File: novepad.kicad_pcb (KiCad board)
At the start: 4 copper layers, 99 x 58 mm, 142 parts, among them J101 NOVENA_LCD_CONN, J102 LP097QX1_CONN, J401 MOLEX_502250-8037, J402 MOLEX_502250-8037, U201 TPS61181, U202 TPS61181, U301 IT6251, U401 FT5816LPC, X301 27MHz 50ppm, 8-18pF, ESR < 80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, X401 12MHz 18pF

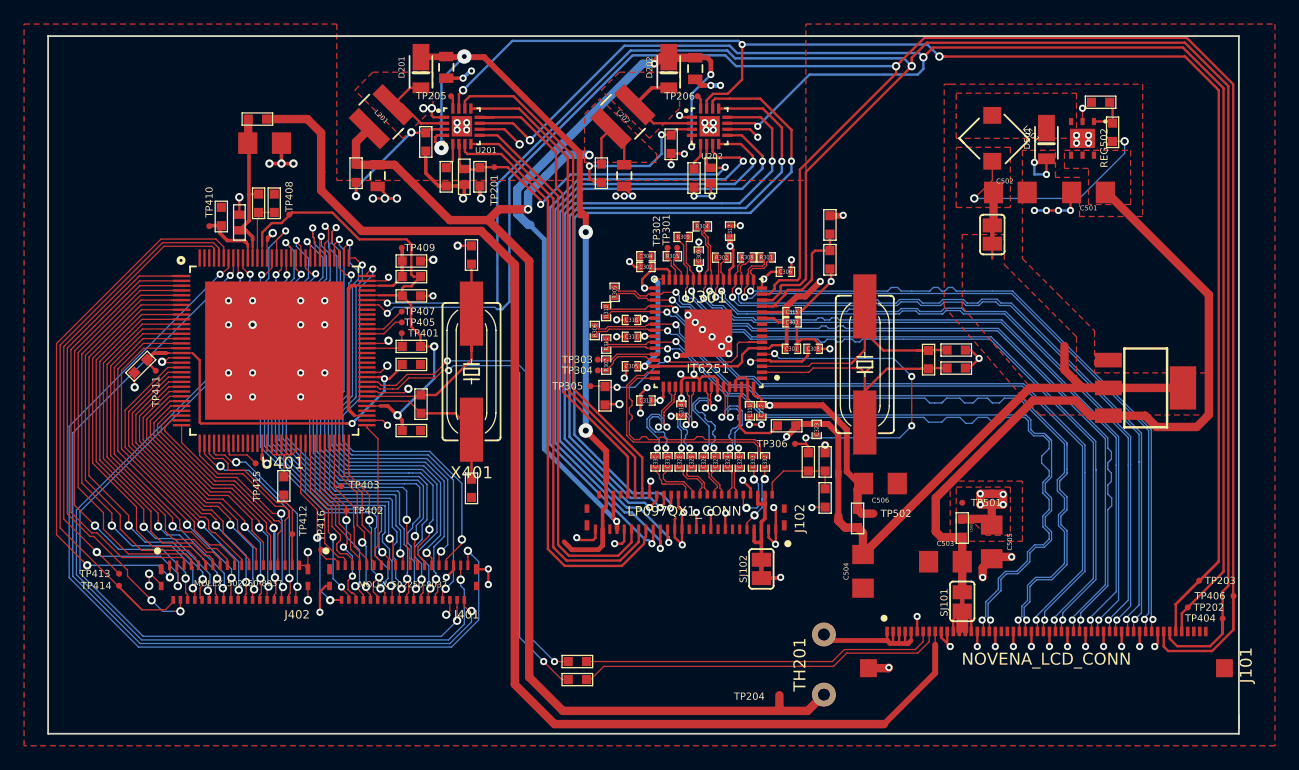
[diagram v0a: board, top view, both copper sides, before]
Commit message: Update silkscreen, check solder paste layers
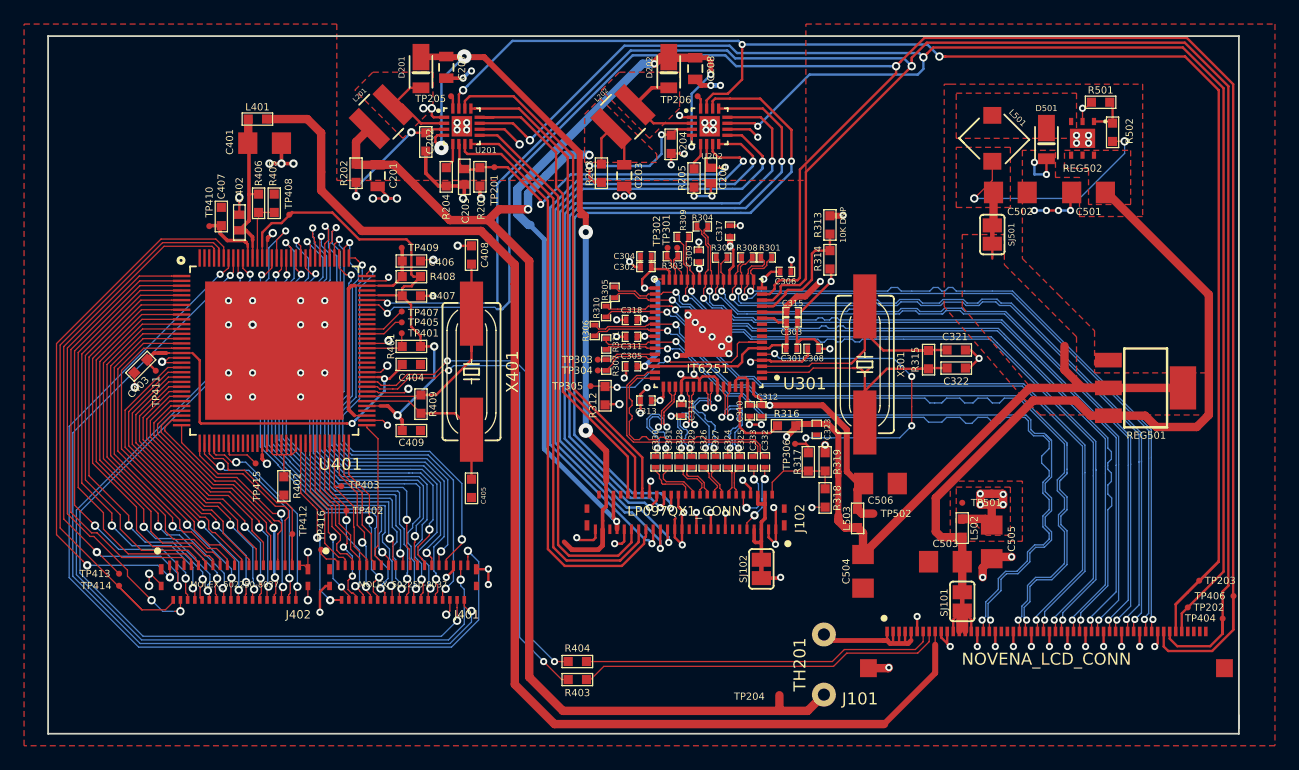
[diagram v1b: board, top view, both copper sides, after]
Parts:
- J101: footprint novepad:MOLEX_51926_5494 -> MOLEX_51926_5494
- J102: footprint novepad:MOLEX_502250_8051 -> MOLEX_502250_8051
- J401: footprint novepad:MOLEX_502250_8037 -> MOLEX_502250_8037
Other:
- rule pad_to_mask_clearance: 0.2 -> 0

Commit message: Minor pcb cleanups
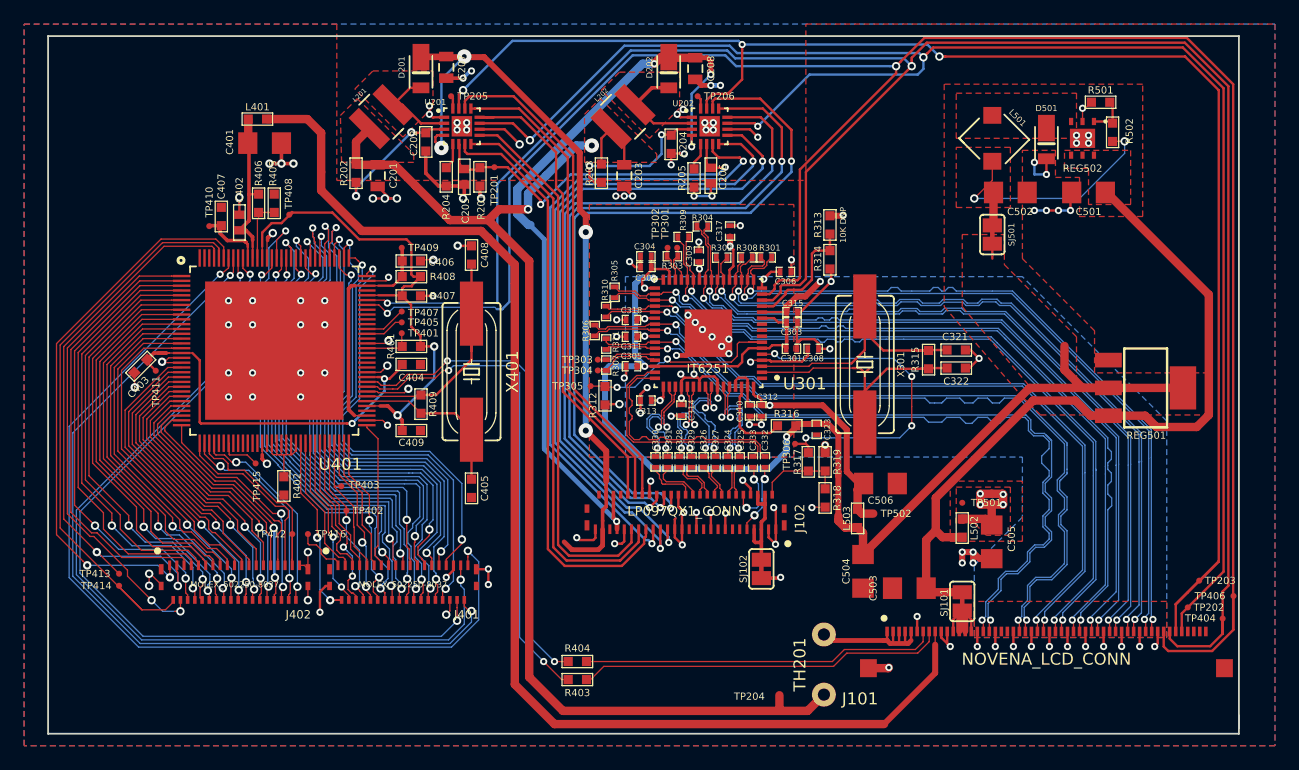
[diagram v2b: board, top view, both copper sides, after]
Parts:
- moved C503 3.72 mm to (157.6, 142.9)
- moved TP416 1.70 mm to (107.6, 138.4)
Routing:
- net +1.8V: track 120.0 -> 111.1 mm
- net +3.3VP: track 59.3 -> 63.0 mm
- net GND: track 247.4 -> 250.6 mm, vias 129 -> 132
- net /Capacitive Touch (Optional)/TEST: track 2.30 -> 4.41 mm
- net /Backlight Driver/VBAT: track 101.8 -> 102.4 mm
- added copper zone on B.Cu, net GND

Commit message: More cleanup, Stencil8 mounting holes
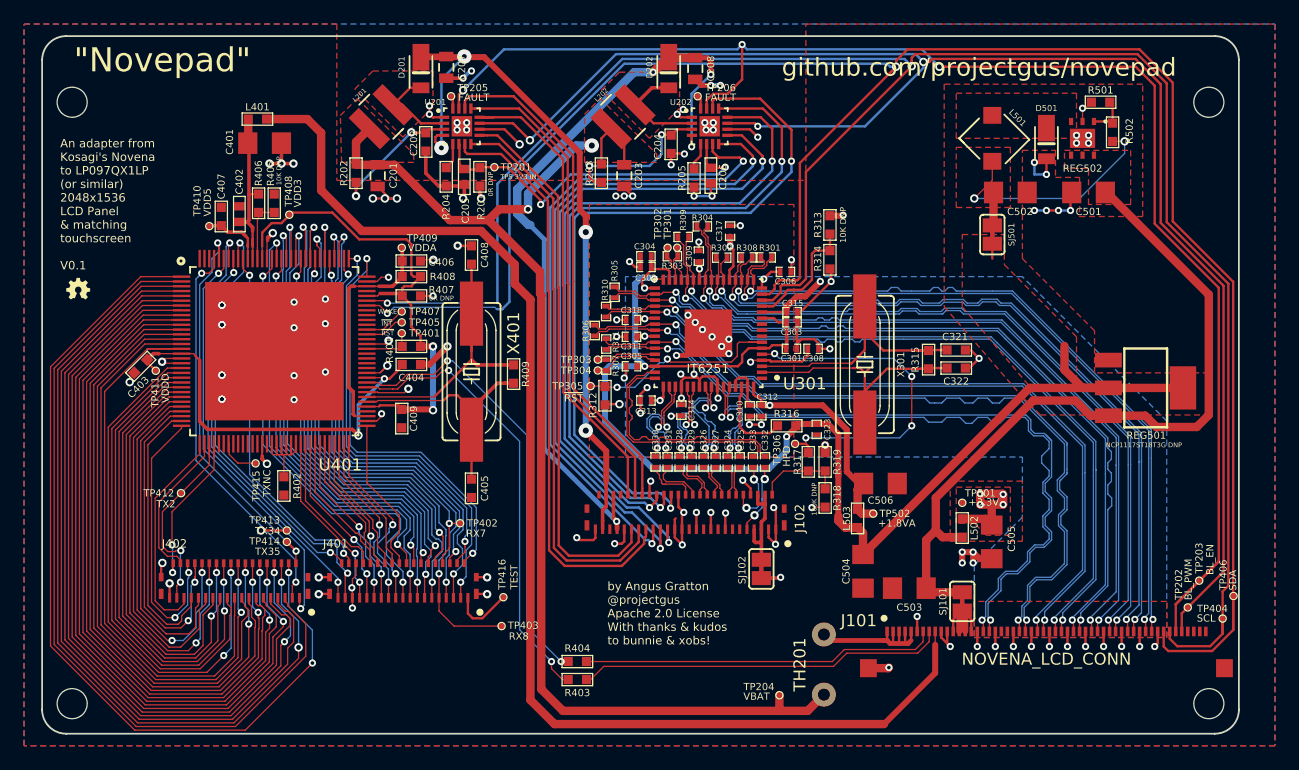
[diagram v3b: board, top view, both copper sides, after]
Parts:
- added LOGO_OSHW_silkscreen_2mm: val**, FT:LOGO_OSHW_silkscreen_2mm, F.Cu at (88.5, 118.0)
- added STENCIL8_HOLE: VAL**, novepad:STENCIL8_HOLE, F.Cu at (88.0, 152.5)
- added STENCIL8_HOLE: VAL**, novepad:STENCIL8_HOLE, F.Cu at (88.0, 102.5)
- added STENCIL8_HOLE: VAL**, novepad:STENCIL8_HOLE, F.Cu at (182.5, 102.5)
- added STENCIL8_HOLE: VAL**, novepad:STENCIL8_HOLE, F.Cu at (182.5, 152.5)
- moved TP403 17.7 mm to (123.7, 146.1)
- moved TP416 17.1 mm to (123.8, 143.7), turned to 90 degrees
- moved TP414 14.4 mm to (105.8, 139.1)
- moved TP413 14.4 mm to (105.8, 138.1)
- moved TP412 9.86 mm to (97.0, 135.0)
- moved TP402 9.51 mm to (120.2, 137.5)
- moved R409 8.10 mm to (124.7, 125.1)
- moved J401 2.70 mm to (115.5, 143.7), turned to 180 degrees
- moved J402 2.70 mm to (101.5, 143.7), turned to 180 degrees
- moved C409 1.28 mm to (115.4, 128.8), turned to 270 degrees
- moved C402 0.70 mm to (101.9, 111.8)
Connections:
- U401 pad 100: /Capacitive Touch (Optional)/RX26 -> /Capacitive Touch (Optional)/RX5
- U401 pad 101: /Capacitive Touch (Optional)/RX25 -> /Capacitive Touch (Optional)/RX6
- U401 pad 102: /Capacitive Touch (Optional)/RX24 -> /Capacitive Touch (Optional)/RX7
- U401 pad 103: /Capacitive Touch (Optional)/RX23 -> /Capacitive Touch (Optional)/RX8
- U401 pad 104: /Capacitive Touch (Optional)/RX22 -> /Capacitive Touch (Optional)/RX9
- U401 pad 105: /Capacitive Touch (Optional)/RX21 -> /Capacitive Touch (Optional)/RX10
- U401 pad 106: /Capacitive Touch (Optional)/RX20 -> /Capacitive Touch (Optional)/RX11
- U401 pad 107: /Capacitive Touch (Optional)/RX19 -> /Capacitive Touch (Optional)/RX12
- U401 pad 108: /Capacitive Touch (Optional)/RX18 -> /Capacitive Touch (Optional)/RX13
- U401 pad 109: /Capacitive Touch (Optional)/RX17 -> /Capacitive Touch (Optional)/RX14
- U401 pad 110: /Capacitive Touch (Optional)/RX16 -> /Capacitive Touch (Optional)/RX15
- U401 pad 111: /Capacitive Touch (Optional)/RX15 -> /Capacitive Touch (Optional)/RX16
- U401 pad 112: /Capacitive Touch (Optional)/RX14 -> /Capacitive Touch (Optional)/RX17
- U401 pad 113: /Capacitive Touch (Optional)/RX13 -> /Capacitive Touch (Optional)/RX18
- U401 pad 54: /Capacitive Touch (Optional)/RX1 -> /Capacitive Touch (Optional)/RX30
- U401 pad 55: /Capacitive Touch (Optional)/RX2 -> /Capacitive Touch (Optional)/RX29
- U401 pad 56: /Capacitive Touch (Optional)/RX3 -> /Capacitive Touch (Optional)/RX28
- U401 pad 57: /Capacitive Touch (Optional)/RX4 -> /Capacitive Touch (Optional)/RX27
- U401 pad 58: /Capacitive Touch (Optional)/RX5 -> /Capacitive Touch (Optional)/RX26
- U401 pad 59: /Capacitive Touch (Optional)/RX6 -> /Capacitive Touch (Optional)/RX25
- U401 pad 60: /Capacitive Touch (Optional)/RX7 -> /Capacitive Touch (Optional)/RX24
- U401 pad 61: /Capacitive Touch (Optional)/RX8 -> /Capacitive Touch (Optional)/RX23
- U401 pad 62: /Capacitive Touch (Optional)/RX9 -> /Capacitive Touch (Optional)/RX22
- U401 pad 63: /Capacitive Touch (Optional)/RX10 -> /Capacitive Touch (Optional)/RX21
- U401 pad 64: /Capacitive Touch (Optional)/RX11 -> /Capacitive Touch (Optional)/RX20
- U401 pad 65: /Capacitive Touch (Optional)/RX12 -> /Capacitive Touch (Optional)/RX19
- U401 pad 96: /Capacitive Touch (Optional)/RX30 -> /Capacitive Touch (Optional)/RX1
- U401 pad 97: /Capacitive Touch (Optional)/RX29 -> /Capacitive Touch (Optional)/RX2
- U401 pad 98: /Capacitive Touch (Optional)/RX28 -> /Capacitive Touch (Optional)/RX3
- U401 pad 99: /Capacitive Touch (Optional)/RX27 -> /Capacitive Touch (Optional)/RX4
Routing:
- net /Capacitive Touch (Optional)/TX37: track 76.8 -> 36.1 mm
- net /Capacitive Touch (Optional)/TX38: track 70.4 -> 31.3 mm
- net /Capacitive Touch (Optional)/TX40: track 68.1 -> 30.5 mm
- net /Capacitive Touch (Optional)/RX8: track 11.9 -> 46.6 mm, vias 0 -> 2
- net /Capacitive Touch (Optional)/TX39: track 72.1 -> 37.7 mm
- net /Capacitive Touch (Optional)/TX33: track 40.3 -> 73.3 mm
- net /Capacitive Touch (Optional)/TX32: track 36.6 -> 68.3 mm
- net /Capacitive Touch (Optional)/RX25: track 43.4 -> 11.8 mm, vias 2 -> 0
- net /Capacitive Touch (Optional)/TX31: track 37.9 -> 69.4 mm
- net /Capacitive Touch (Optional)/RX10: track 11.2 -> 41.9 mm, vias 0 -> 2
- net /Capacitive Touch (Optional)/TX30: track 35.1 -> 65.0 mm
- net /Capacitive Touch (Optional)/TX29: track 36.6 -> 66.3 mm
- net /Capacitive Touch (Optional)/RX23: track 41.2 -> 11.7 mm, vias 2 -> 0
- net /Capacitive Touch (Optional)/RX21: track 40.6 -> 11.6 mm, vias 2 -> 0
- net /Capacitive Touch (Optional)/TX28: track 33.5 -> 62.3 mm
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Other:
- board size 99 x 58 mm -> 99.5 x 58 mm
- rule pad_to_mask_clearance: 0 -> 0.025
- board text added: ""Novepad""
- board text added: "+1.8VA"
- board text added: "+3.3V"
- board text added: "An adapter from Kosagi's Novena to LP097QX1LP (or similar) 2048x1536 LCD Panel & matching touchscreen V0.1"
- board text added: "BL_EN"
- board text added: "BL_PWM"
- board text added: "FAULT"
- board text added: "HPD"
- board text added: "RX7"
- board text added: "RX8"
- board text added: "SCL"
- board text added: "SDA"
- board text added: "TEST"
- board text added: "TPS 3V3 IN"
- board text added: "TX2"
- board text added: "TX34"
- board text added: "TX35"
- board text added: "TXNC"
- board text added: "VBAT"
- board text added: "VDD3"
- board text added: "VDD5"
- board text added: "VDDA"
- board text added: "VDDD"
- board text added: "WAKE"
- board text added: "by Angus Gratton @projectgus Apache 2.0 License With thanks & kudos to bunnie & xobs!"
- board text added: "github.com/projectgus/novepad"
- board text added: "~INT"
- board text added: "~RST"

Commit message: More cleanup
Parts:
- added TP307: CONN_1, novepad:SMD_TEST_POINT, F.Cu at (146.3, 122.1)
- added TP308: CONN_1, novepad:SMD_TEST_POINT, F.Cu at (147.2, 121.7)
- added TP309: CONN_1, novepad:SMD_TEST_POINT, F.Cu at (146.3, 121.0)
- moved J401 0.30 mm to (115.2, 143.7)
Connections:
- C323 pad 1: +1.8V -> +1.8VA
- R316 pad 1: +1.8V -> +1.8VA
- U301 pad 10: (no net) -> Net-(TP309-Pad1)
- U301 pad 8: (no net) -> Net-(TP307-Pad1)
- U301 pad 9: (no net) -> Net-(TP308-Pad1)
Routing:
- net +1.8VA: track 56.8 -> 60.5 mm
- net +1.8V: track 111.1 -> 114.5 mm
- net Net-(TP308-Pad1): track 0.00 -> 1.90 mm
- net Net-(TP307-Pad1): track 0.00 -> 1.06 mm
- net Net-(TP309-Pad1): track 0.00 -> 1.02 mm
- net /Capacitive Touch (Optional)/RX1: track 35.3 -> 35.9 mm
- net /Capacitive Touch (Optional)/RX2: track 37.1 -> 37.7 mm
- net GND: track 253.8 -> 253.4 mm, vias 131 -> 130

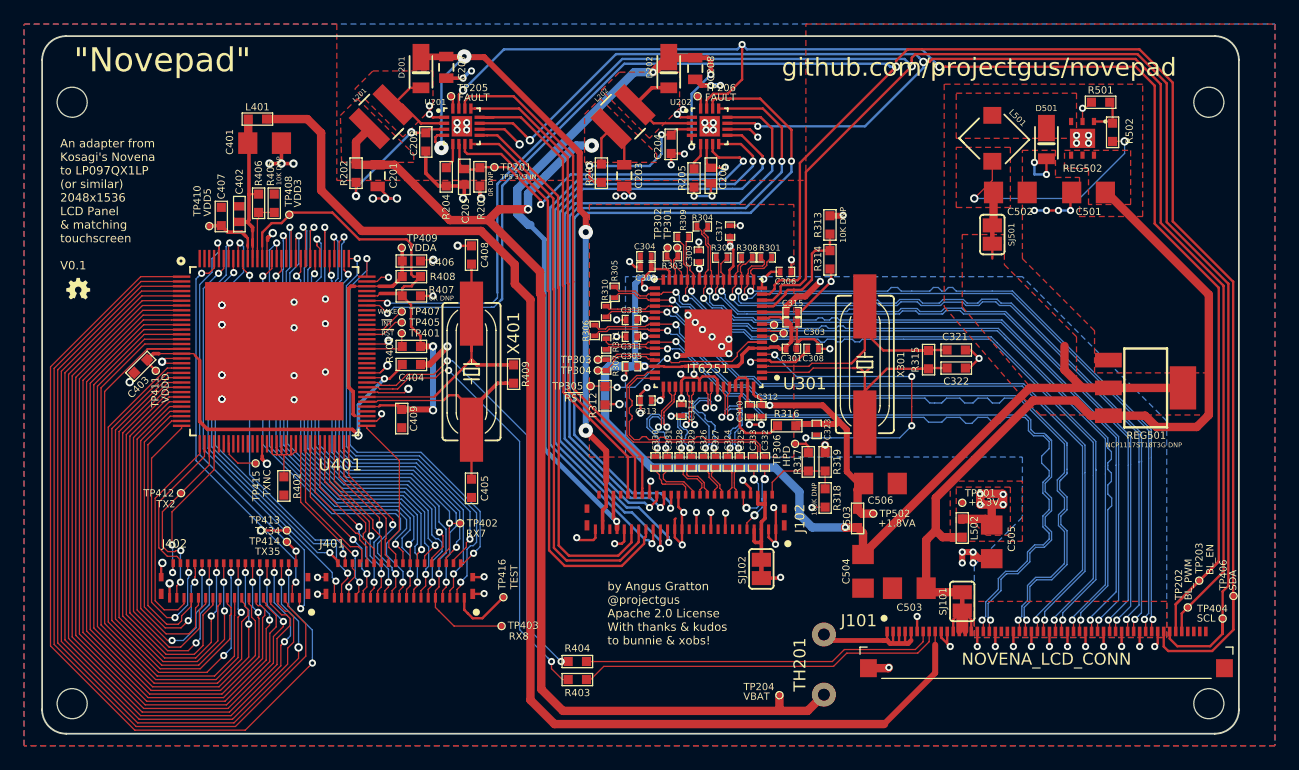
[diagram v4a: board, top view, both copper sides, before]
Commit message: Fix characteristic impedance, no longer require 4/4 trace/space, as per notes in README
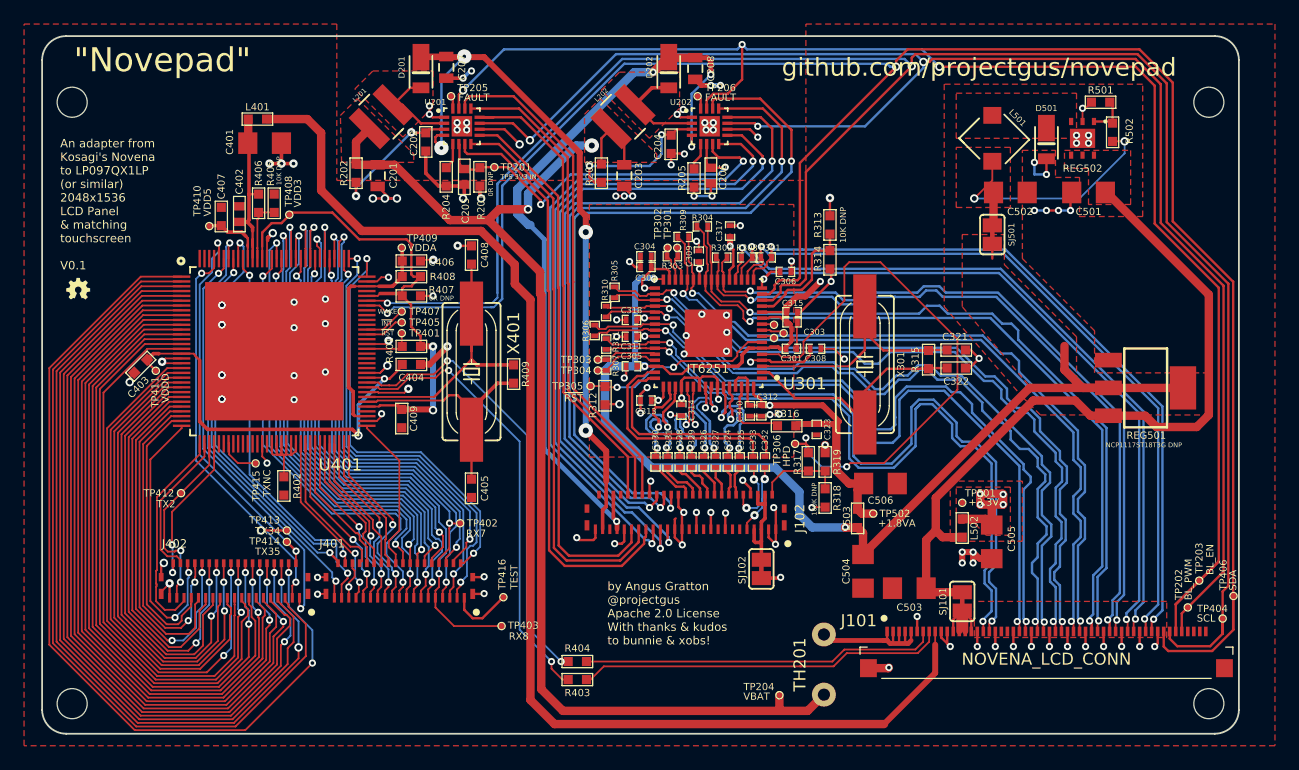
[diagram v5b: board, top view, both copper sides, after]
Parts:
- moved C308 0.20 mm to (149.8, 123.0)
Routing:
- net /LVDS to eDP Conversion/HPD: track 28.8 -> 47.8 mm, vias 4 -> 2
- net GND: track 253.4 -> 258.2 mm, vias 130 -> 128
- net Net-(C322-Pad1): track 26.6 -> 22.9 mm
- net /Capacitive Touch (Optional)/TX18: track 48.2 -> 45.4 mm
- net /LVDS to eDP Conversion/LVDS0_3_N: track 62.8 -> 60.4 mm
- net /LVDS to eDP Conversion/LVDS1_2_P: track 63.1 -> 60.8 mm
- net /LVDS to eDP Conversion/LVDS1_0_P: track 62.8 -> 60.5 mm
- net /LVDS to eDP Conversion/LVDS1_0_N: track 62.9 -> 60.7 mm
- net /LVDS to eDP Conversion/LVDS1_2_N: track 63.1 -> 61.1 mm
- net /LVDS to eDP Conversion/LVDS0_3_P: track 63.0 -> 61.1 mm
- net /LVDS to eDP Conversion/LVDS0_0_N: track 60.0 -> 61.7 mm
- net /LVDS to eDP Conversion/LVDS1_3_P: track 62.3 -> 60.6 mm
- net Net-(C321-Pad1): track 23.3 -> 24.8 mm
- net /LVDS to eDP Conversion/LVDS1_1_P: track 61.5 -> 60.1 mm
- net /LVDS to eDP Conversion/LVDS0_0_P: track 60.1 -> 61.4 mm
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- removed copper zone on B.Cu, net GND
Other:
- net class Backlight: clearance 0.2 -> 0.15; trace_width 0.3 -> 0.2; via_dia 0.7 -> 0.6; via_drill 0.4 -> 0.3
- net class Default: clearance 0.2 -> 0.15; trace_width 0.2 -> 0.15; via_dia 0.7 -> 0.6; via_drill 0.4 -> 0.3
- net class LVDS_DP1/3: clearance 0.1 -> 0.15; trace_width 0.1 -> 0.175
- net class LVDS_Unused: clearance 0.1 -> 0.15; trace_width 0.1 -> 0.175; via_dia 0.7 -> 0.6; via_drill 0.4 -> 0.3
- net class Power: clearance 0.2 -> 0.15; via_dia 1.2 -> 0.7; via_drill 0.5 -> 0.4
- net class eDP_ACC_DP0.1/2 removed
- net class eDP_ACC_DP0.2/5 added: clearance 0.15, trace_width 0.175, via_dia 0.6, via_drill 0.3
- net class eDP_AUX_DP0.2/3 removed
- net class eDP_AUX_DP0.2/5 added: clearance 0.15, trace_width 0.175, via_dia 0.6, via_drill 0.3
- net class eDP_AUX_OUT_DP0.2/2 removed
- net class eDP_AUX_OUT_DP0.2/5 added: clearance 0.15, trace_width 0.175, via_dia 0.6, via_drill 0.3
- net class eDP_DP0.2/2 removed
- net class eDP_DP0.2/5 added: clearance 0.15, trace_width 0.175, via_dia 0.6, via_drill 0.3
- rule trace_clearance: 0.2 -> 0.15
- rule trace_min: 0.1 -> 0.15
